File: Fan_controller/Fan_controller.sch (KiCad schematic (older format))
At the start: 14 parts, among them J1 Conn_01x04, J2 Conn_01x04, J3 Conn_01x04, J4 Conn_01x04, J5 Conn_01x04, U1 STM32F103RETx

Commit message: Add MOSFETs
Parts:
- added Q1, Q2, Q3, Q4, Q5: IRLZ44N, Package_TO_SOT_THT:TO-220-3_Vertical, symbol Transistor_FET:IRLZ44N
- R1: value R -> 1K
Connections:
- net GNDREF: now also J1.4 (Pin_4), J2.4 (Pin_4), J3.4 (Pin_4), J4.4 (Pin_4), J5.4 (Pin_4), Q1.3 (S), Q2.3 (S), Q3.3 (S), Q4.3 (S), Q5.3 (S)
- net +12V: now reaches J1.1 (Pin_1)
- net +12V: now also J2.1 (Pin_1), J3.1 (Pin_1), J4.1 (Pin_1), J5.1 (Pin_1)
- net at J1.2 (Pin_2): now also Q1.2 (D)
- net at J2.2 (Pin_2): now also Q2.2 (D)
- net at J3.2 (Pin_2): now also Q3.2 (D)
- net at J4.2 (Pin_2): now also Q4.2 (D)
- net at J5.2 (Pin_2): now also Q5.2 (D)
- new net CH1: Q1.1 (G)
- new net CH2: Q2.1 (G)
- new net CH3: Q3.1 (G)
- new net CH4: Q4.1 (G)
- new net CH5: Q5.1 (G)
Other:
- moved on the sheet: J1

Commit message: add USB connector, add LDO
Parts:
- added C?: 10uF, symbol Device:CP1
- added C?: 22uF, symbol Device:CP1
- added J?: ATX_USB, symbol Connector_Generic:Conn_01x05
- added U?: AMS1117-3.3, Package_TO_SOT_SMD:SOT-223-3_TabPin2, symbol Regulator_Linear:AMS1117-3.3
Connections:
- net GNDREF: now also C?.2, C?.2, J?.4 (Pin_4), U?.1 (GND); no longer J1.4 (Pin_4), J2.4 (Pin_4), J3.4 (Pin_4), J4.4 (Pin_4), J5.4 (Pin_4)
- net +3V3 renamed +3.3v
- net +3.3v: now also C?.1, U?.2 (VO)
- new net +5V: C?.1, J?.1 (Pin_1), U?.3 (VI)
- new net D+: J?.3 (Pin_3)
- new net D-: J?.2 (Pin_2)
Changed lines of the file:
@@
 	5150 1000 5250 1000
-Wire Wire Line
-	5050 1000 5050 850
-Connection ~ 5050 1000
-$Comp
-L power:+3.3V #PWR04
-U 1 1 5C6DCAD2
-P 5050 850
-F 0 "#PWR04" H 5050 700 50  0001 C CNN
-F 1 "+3.3V" H 5065 1023 50  0000 C CNN
-F 2 "" H 5050 850 50  0001 C CNN
-F 3 "" H 5050 850 50  0001 C CNN
-	1    5050 850
-	1    0    0    -1
-$EndComp
 Wire Wire Line
 	4950 4700 4950 4800
@@
 F 3 "" H 4050 6350 50  0001 C CNN
 	1    4050 6350
-	1    0    0    -1
-$EndComp
-$Comp
-L power:+3.3V #PWR01
-U 1 1 5C6E93D5
-P 4050 5550
-F 0 "#PWR01" H 4050 5400 50  0001 C CNN
-F 1 "+3.3V" H 4065 5723 50  0000 C CNN
-F 2 "" H 4050 5550 50  0001 C CNN
-F 3 "" H 4050 5550 50  0001 C CNN
-	1    4050 5550
 	1    0    0    -1
 $EndComp
@@
 Wire Wire Line
 	1400 850  1700 850
-Wire Wire Line
-	1400 1150 1700 1150
 $Comp
 L Connector_Generic:Conn_01x04 J2
@@
 Wire Wire Line
 	1400 1400 1700 1400
-Wire Wire Line
-	1400 1700 1700 1700
 $Comp
 L Connector_Generic:Conn_01x04 J3
@@
 Wire Wire Line
 	1400 1950 1700 1950
-Wire Wire Line
-	1400 2250 1700 2250
 $Comp
 L Connector_Generic:Conn_01x04 J4
@@
 Wire Wire Line
 	1400 2500 1700 2500
-Wire Wire Line
-	1400 2800 1700 2800
 $Comp
 L Connector_Generic:Conn_01x04 J5
@@
 Wire Wire Line
 	1400 3050 1700 3050
-Wire Wire Line
-	1400 3350 1700 3350
 $Comp
 L Transistor_FET:IRLZ44N Q5
@@
 L power:+12V #PWR013
 U 1 1 5C750BC6
-P 3200 700
-F 0 "#PWR013" H 3200 550 50  0001 C CNN
-F 1 "+12V" H 3215 873 50  0000 C CNN
-F 2 "" H 3200 700 50  0001 C CNN
-F 3 "" H 3200 700 50  0001 C CNN
-	1    3200 700
-	1    0    0    -1
-$EndComp
-Wire Wire Line
-	3200 700  3200 900
-Text Label 3200 900  1    50   ~ 0
+P 3150 700
+F 0 "#PWR013" H 3150 550 50  0001 C CNN
+F 1 "+12V" H 3165 873 50  0000 C CNN
+F 2 "" H 3150 700 50  0001 C CNN
+F 3 "" H 3150 700 50  0001 C CNN
+	1    3150 700
+	1    0    0    -1
+$EndComp
+Wire Wire Line
+	3150 700  3150 900
+Text Label 3150 900  1    50   ~ 0
 +12v
 $Comp
@@
 F 3 "" H 2650 3350 50  0001 C CNN
 	1    2650 3350
-	1    0    0    -1
-$EndComp
-$Comp
-L power:GNDREF #PWR011
-U 1 1 5C75523C
-P 1700 3350
-F 0 "#PWR011" H 1700 3100 50  0001 C CNN
-F 1 "GNDREF" H 1705 3177 50  0000 C CNN
-F 2 "" H 1700 3350 50  0001 C CNN
-F 3 "" H 1700 3350 50  0001 C CNN
-	1    1700 3350
-	1    0    0    -1
-$EndComp
-$Comp
-L power:GNDREF #PWR010
-U 1 1 5C75683F
-P 1700 2800
-F 0 "#PWR010" H 1700 2550 50  0001 C CNN
-F 1 "GNDREF" H 1705 2627 50  0000 C CNN
-F 2 "" H 1700 2800 50  0001 C CNN
-F 3 "" H 1700 2800 50  0001 C CNN
-	1    1700 2800
-	1    0    0    -1
-$EndComp
-$Comp
-L power:GNDREF #PWR09
-U 1 1 5C757E42
-P 1700 2250
-F 0 "#PWR09" H 1700 2000 50  0001 C CNN
-F 1 "GNDREF" H 1705 2077 50  0000 C CNN
-F 2 "" H 1700 2250 50  0001 C CNN
-F 3 "" H 1700 2250 50  0001 C CNN
-	1    1700 2250
-	1    0    0    -1
-$EndComp
-$Comp
-L power:GNDREF #PWR08
-U 1 1 5C7595FA
-P 1700 1700
-F 0 "#PWR08" H 1700 1450 50  0001 C CNN
-F 1 "GNDREF" H 1705 1527 50  0000 C CNN
-F 2 "" H 1700 1700 50  0001 C CNN
-F 3 "" H 1700 1700 50  0001 C CNN
-	1    1700 1700
-	1    0    0    -1
-$EndComp
-$Comp
-L power:GNDREF #PWR07
-U 1 1 5C75ABFD
-P 1700 1150
-F 0 "#PWR07" H 1700 900 50  0001 C CNN
-F 1 "GNDREF" H 1705 977 50  0000 C CNN
-F 2 "" H 1700 1150 50  0001 C CNN
-F 3 "" H 1700 1150 50  0001 C CNN
-	1    1700 1150
 	1    0    0    -1
 $EndComp
@@
 	2650 3350 2650 3150
 Connection ~ 2650 3150
+$Comp
+L Connector_Generic:Conn_01x05 J?
+U 1 1 5C7328D6
+P 9250 1150
+F 0 "J?" H 9330 1192 50  0000 L CNN
+F 1 "ATX_USB" H 9330 1101 50  0000 L CNN
+F 2 "" H 9250 1150 50  0001 C CNN
+F 3 "~" H 9250 1150 50  0001 C CNN
+	1    9250 1150
+	1    0    0    -1
+$EndComp
+Wire Wire Line
+	9050 950  8700 950
+Wire Wire Line
+	9050 1050 8700 1050
+Wire Wire Line
+	9050 1150 8700 1150
+Wire Wire Line
+	9050 1250 8700 1250
+Text Label 8700 950  0    50   ~ 0
++5v
+Text Label 8700 1050 0    50   ~ 0
+D-
+Text Label 8700 1150 0    50   ~ 0
+D+
+Wire Wire Line
+	3350 6150 3350 6350
+$Comp
+L power:GNDREF #PWR?
+U 1 1 5C7403D1
+P 3350 6350
+F 0 "#PWR?" H 3350 6100 50  0001 C CNN
+F 1 "GNDREF" H 3355 6177 50  0000 C CNN
+F 2 "" H 3350 6350 50  0001 C CNN
+F 3 "" H 3350 6350 50  0001 C CNN
+	1    3350 6350
+	1    0    0    -1
+$EndComp
+Text Label 3350 6150 3    50   ~ 0
+GND
+Text Label 8700 1250 0    50   ~ 0
+GND
+$Comp
+L power:+5V #PWR?
+U 1 1 5C747585
+P 6700 800
+F 0 "#PWR?" H 6700 650 50  0001 C CNN
+F 1 "+5V" H 6715 973 50  0000 C CNN
+F 2 "" H 6700 800 50  0001 C CNN
+F 3 "" H 6700 800 50  0001 C CNN
+	1    6700 800
+	1    0    0    -1
+$EndComp
+Wire Wire Line
+	6700 800  6700 1000
+Text Label 6700 1000 1    50   ~ 0
++5v
+Wire Wire Line
+	4050 5300 4050 5550
+Text Label 4050 5300 3    50   ~ 0
++3.3v
+$Comp
+L Regulator_Linear:AMS1117-3.3 U?
+U 1 1 5C75DBFF
+P 7200 1000
+F 0 "U?" H 7200 1242 50  0000 C CNN
+F 1 "AMS1117-3.3" H 7200 1151 50  0000 C CNN
+F 2 "Package_TO_SOT_SMD:SOT-223-3_TabPin2" H 7200 1200 50  0001 C CNN
+F 3 "http://www.advanced-monolithic.com/pdf/ds1117.pdf" H 7300 750 50  0001 C CNN
+	1    7200 1000
+	1    0    0    -1
+$EndComp
+Wire Wire Line
+	6700 1000 6900 1000
+Wire Wire Line
+	7200 1300 7200 1500
+$Comp
+L Device:CP1 C?
+U 1 1 5C765DA1
+P 6700 1250
+F 0 "C?" H 6815 1296 50  0000 L CNN
+F 1 "10uF" H 6815 1205 50  0000 L CNN
+F 2 "" H 6700 1250 50  0001 C CNN
+F 3 "~" H 6700 1250 50  0001 C CNN
+	1    6700 1250
+	1    0    0    -1
+$EndComp
+Wire Wire Line
+	7500 1000 7650 1000
+$Comp
+L Device:CP1 C?
+U 1 1 5C767DBE
+P 7650 1250
+F 0 "C?" H 7765 1296 50  0000 L CNN
+F 1 "22uF" H 7765 1205 50  0000 L CNN
+F 2 "" H 7650 1250 50  0001 C CNN
+F 3 "~" H 7650 1250 50  0001 C CNN
+	1    7650 1250
+	1    0    0    -1
+$EndComp
+Wire Wire Line
+	7650 1100 7650 1000
+Wire Wire Line
+	6700 1100 6700 1000
+Connection ~ 6700 1000
+Wire Wire Line
+	6700 1400 6700 1500
+Wire Wire Line
+	6700 1500 7200 1500
+Wire Wire Line
+	7200 1500 7650 1500
+Wire Wire Line
+	7650 1500 7650 1400
+Connection ~ 7200 1500
+$Comp
+L power:GNDREF #PWR?
+U 1 1 5C7726A9
+P 7200 1650
+F 0 "#PWR?" H 7200 1400 50  0001 C CNN
+F 1 "GNDREF" H 7205 1477 50  0000 C CNN
+F 2 "" H 7200 1650 50  0001 C CNN
+F 3 "" H 7200 1650 50  0001 C CNN
+	1    7200 1650
+	1    0    0    -1
+$EndComp
+Wire Wire Line
+	7200 1500 7200 1650
+Text Label 7650 1000 2    50   ~ 0
++3.3v
+Text Label 5050 1000 0    50   ~ 0
++3.3v
 $EndSCHEMATC

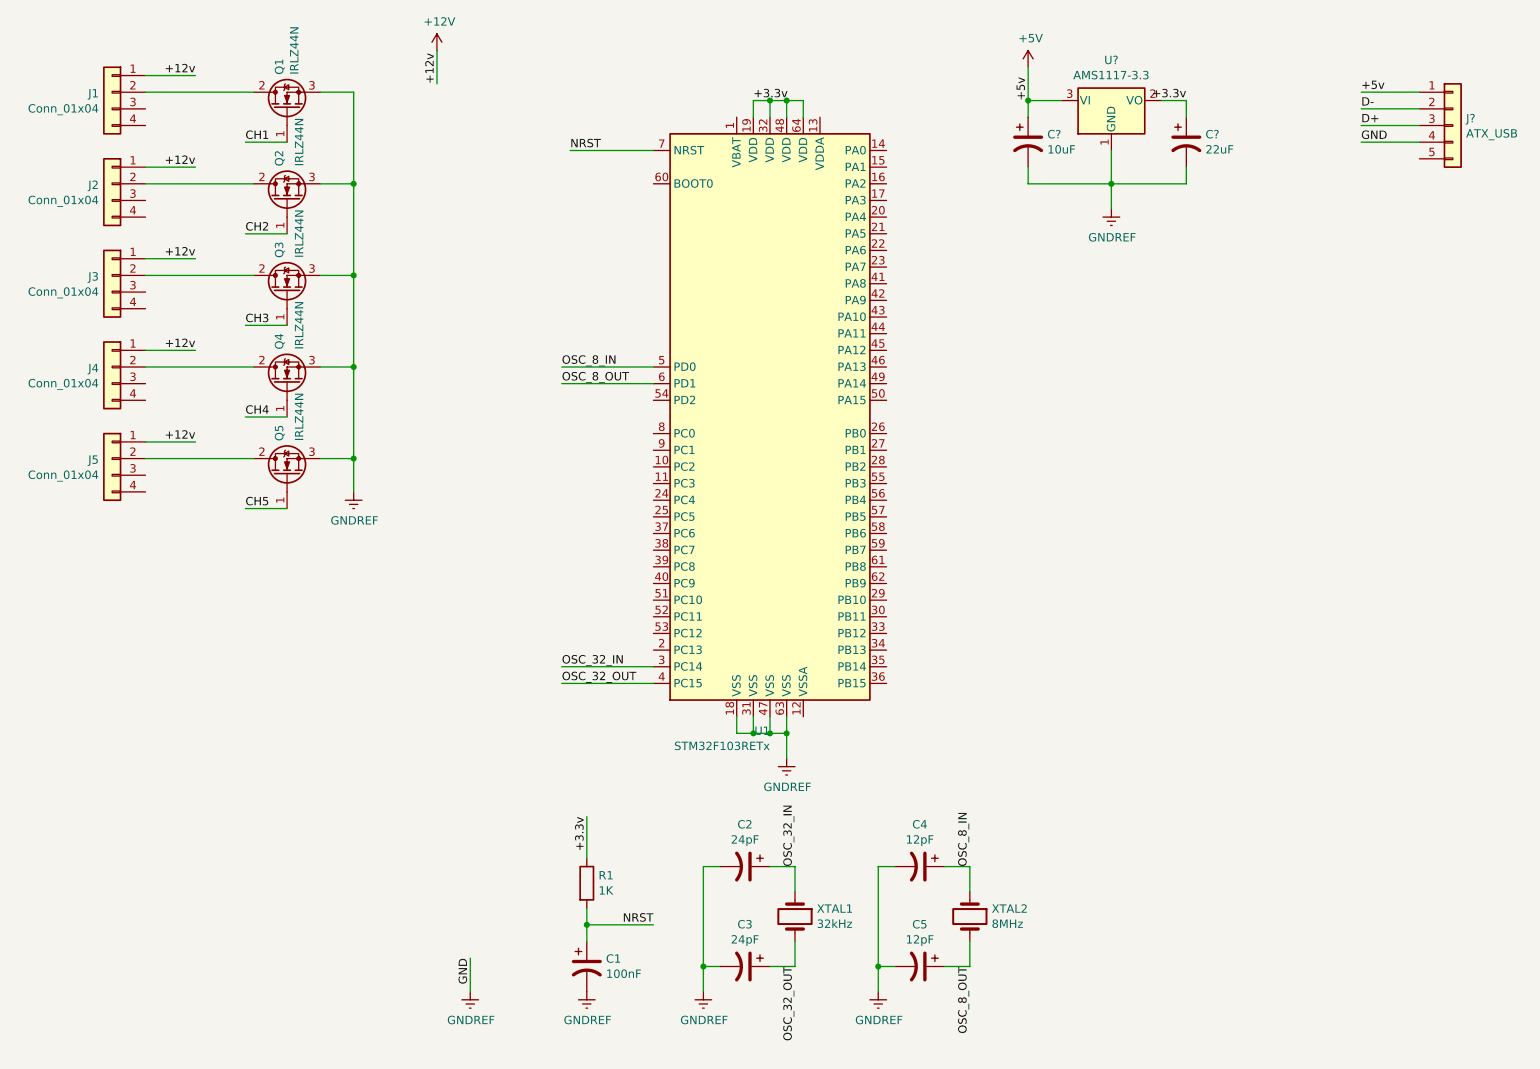
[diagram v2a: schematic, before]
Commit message: add SWD port, NRST button
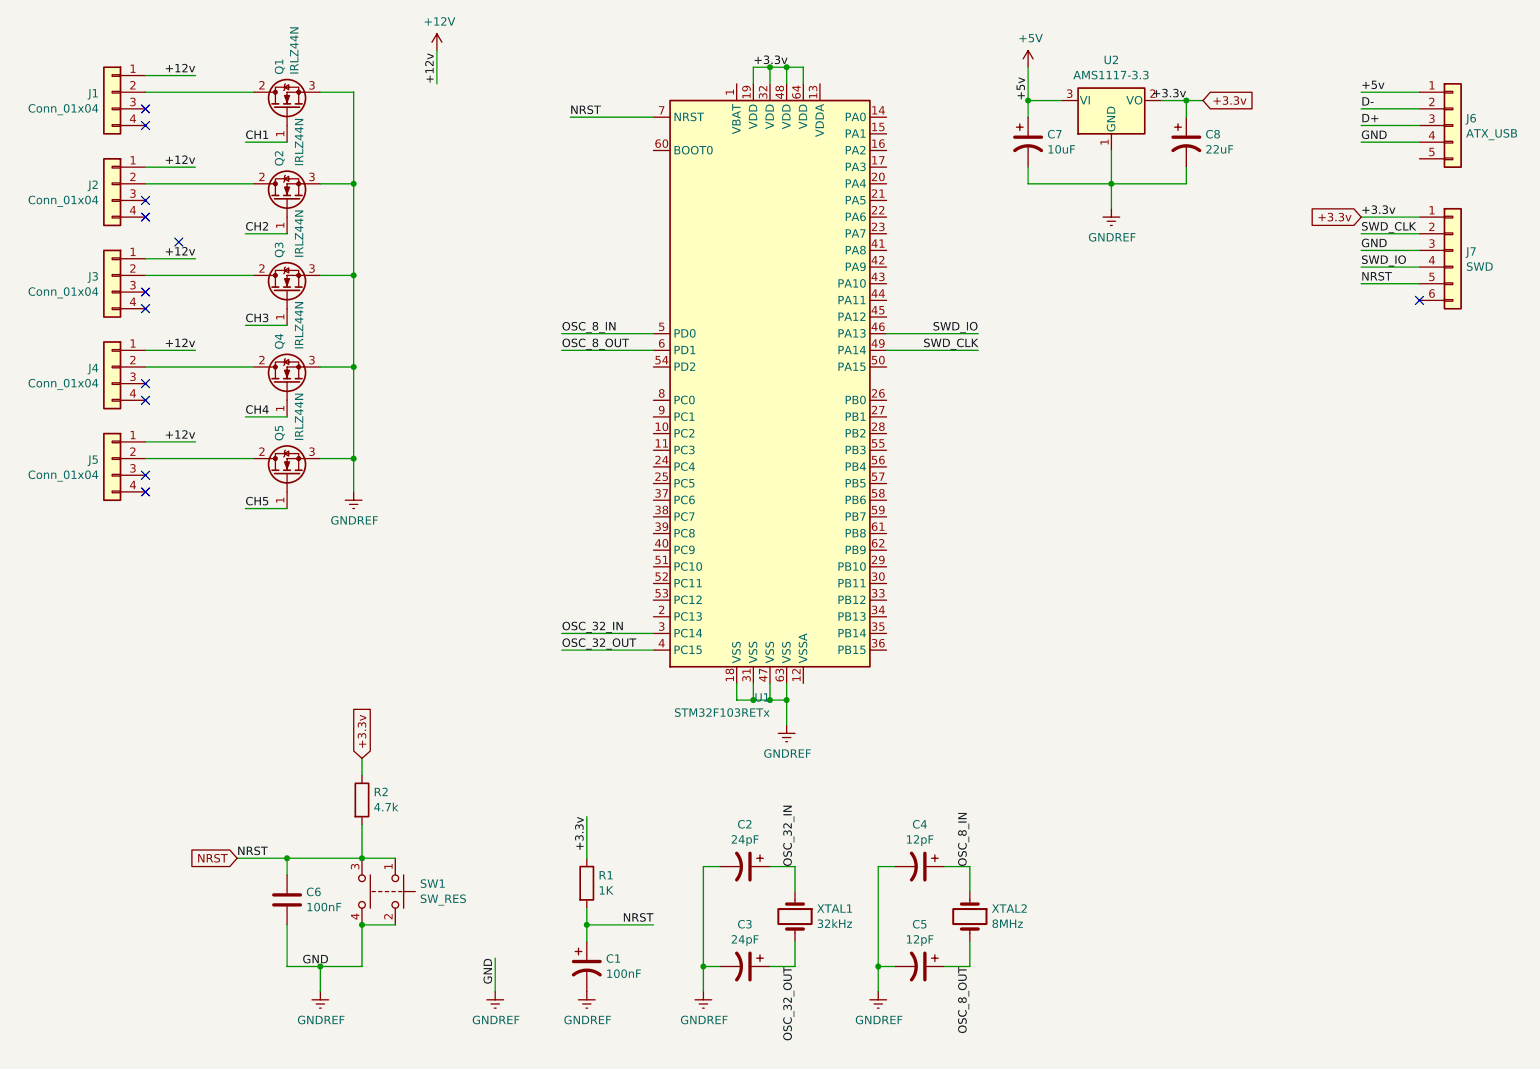
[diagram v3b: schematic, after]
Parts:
- added C6: 100nF, Capacitor_SMD:C_0805_2012Metric, symbol Device:C
- added J7: SWD, Connector_PinHeader_2.54mm:PinHeader_1x06_P2.54mm_Vertical, symbol Connector_Generic:Conn_01x06
- added R2: 4.7k, Resistor_SMD:R_0805_2012Metric_Pad1.15x1.40mm_HandSolder, symbol Device:R
- added SW1: SW_RES, Button_Switch_SMD:SW_SPST_TL3305C, symbol Switch:SW_Push_Dual
- C7, C8: renamed from C?; footprint (none) -> Capacitor_SMD:C_0805_2012Metric
- J6: renamed from J?; footprint (none) -> Connector_PinHeader_2.54mm:PinHeader_1x05_P2.54mm_Vertical
- R1: footprint (none) -> Resistor_SMD:R_0805_2012Metric_Pad1.15x1.40mm_HandSolder
- XTAL1, XTAL2: footprint (none) -> Crystal:Crystal_HC49-4H_Vertical
- gave numbers to parts that had none: 1
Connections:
- net +3.3v: now also J7.1 (Pin_1), R2.1
- net GNDREF: now also C6.2, J7.3 (Pin_3), SW1.2, SW1.4
- net NRST: now also C6.1, J7.5 (Pin_5), R2.2, SW1.1, SW1.3
- net SWD_IO: now reaches U1.46 (PA13)
- net SWD_IO: now also J7.4 (Pin_4)
- net SWD_CLK: now reaches U1.49 (PA14)
- net SWD_CLK: now also J7.2 (Pin_2)
- no-connect marks 0 -> 12
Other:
- moved on the sheet: U1
